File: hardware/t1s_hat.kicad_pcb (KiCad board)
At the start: 4 copper layers, 66.2 x 49.2 mm, 42 parts, among them CN1 T1S BUS P N N P, J1 2x20 socket (riser stack), U1 LAN8651, Y1 25.000MHz CL12

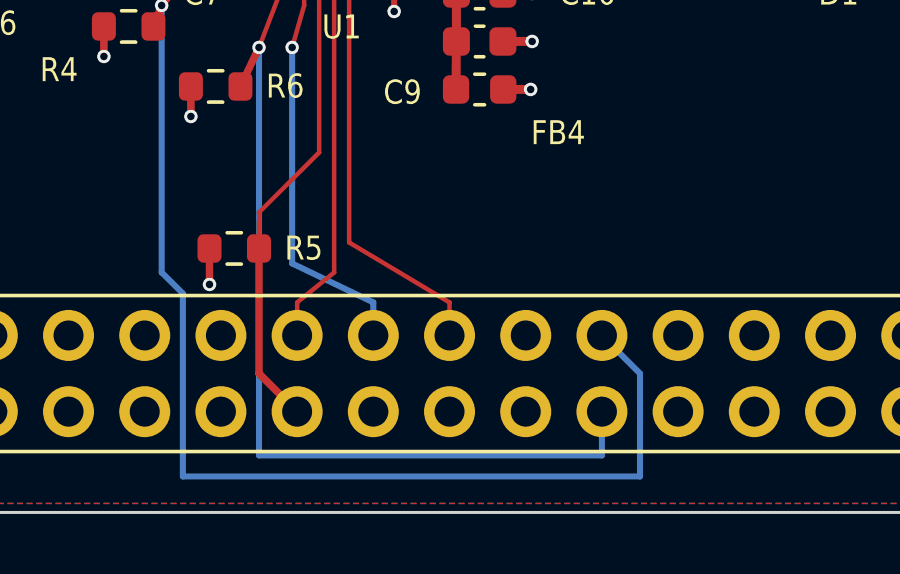
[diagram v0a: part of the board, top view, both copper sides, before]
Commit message: Rev B review follow-ups: X7R CCOMP, probe labels, ferrite note, 23 mm
Checked against the board file and Microchip's documents:
- C4 (CCOMP) X5R -> X7R (Yageo CC0805KKX7R8BB475, C354262). The
  checklist says 'metal film', the data sheet does not; recorded.
- J1 pins 15-24 carry all six host signals plus 3V3 and GND: labelled
  on the silkscreen as the bring-up probe points.
- Ferrite beads need a local 10 uF (checklist); FB1-4 documented as
  0 ohm links, with which the single C6 is compliant.
- Stack height text corrected to the calculated ~23 mm everywhere.
- README 'Review notes': why the P N N P connector stays (the node's
  stub is 15.92 mm on both legs; the difference is the through-bus,
  ~93 ps) and why no series-R on SCLK/MOSI (driver is the ESP32).
DRC 0 errors, ERC 0 errors, mechanical 0.00000 mm.
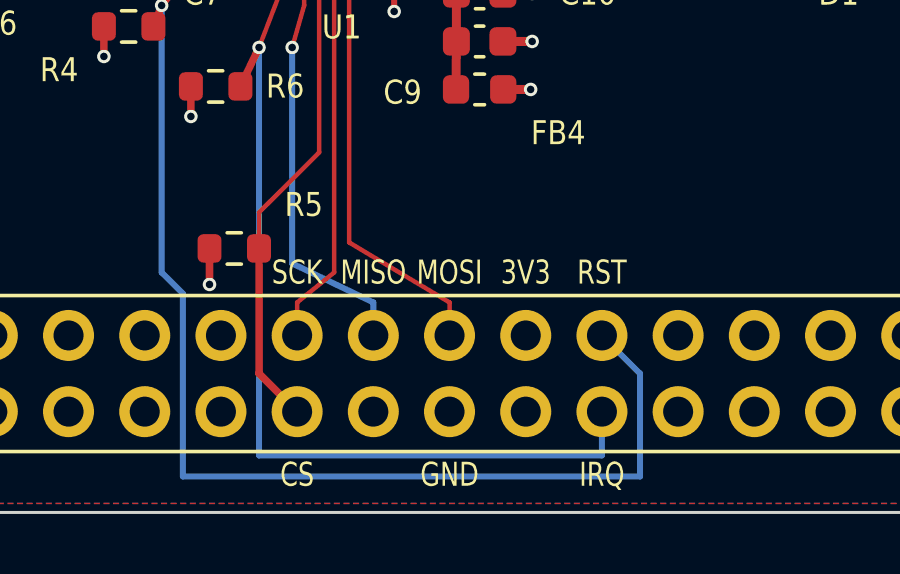
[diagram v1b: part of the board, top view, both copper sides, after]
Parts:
- C4: value 4.7uF low-ESR -> 4.7uF X7R
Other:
- board text added: "3V3"
- board text added: "CS"
- board text added: "GND"
- board text added: "IRQ"
- board text added: "MISO"
- board text added: "MOSI"
- board text added: "RST"
- board text added: "SCK"
